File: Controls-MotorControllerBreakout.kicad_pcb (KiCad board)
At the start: 2 copper layers, 39.2 x 24.8 mm, 16 parts, among them J1 MC CAN 1, J2 MC CAN 2, J3 CAN INTRFC, J4 EXT PWR

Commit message: change diode + models
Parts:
- D2: value 1N4007 -> M7
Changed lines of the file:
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@@
 			)
 		)
-		(property "Value" "1N4007"
+		(property "Value" "M7"
 			(at 0 -2.1 0)
 			(layer "B.Fab")
@@
 			)
 		)
-		(property "Datasheet" "https://www.digikey.com/en/products/detail/smc-diode-solutions/1N4007FL/11657817"
+		(property "Datasheet" "https://www.diodes.com/assets/Datasheets/RS1MWF.pdf"
 			(at 0 0 0)
 			(unlocked yes)
@@
 			)
 		)
-		(property "P/N" "1N4007FL"
+		(property "P/N" "RS1MWF-7"
 			(at 0 0 0)
 			(unlocked yes)

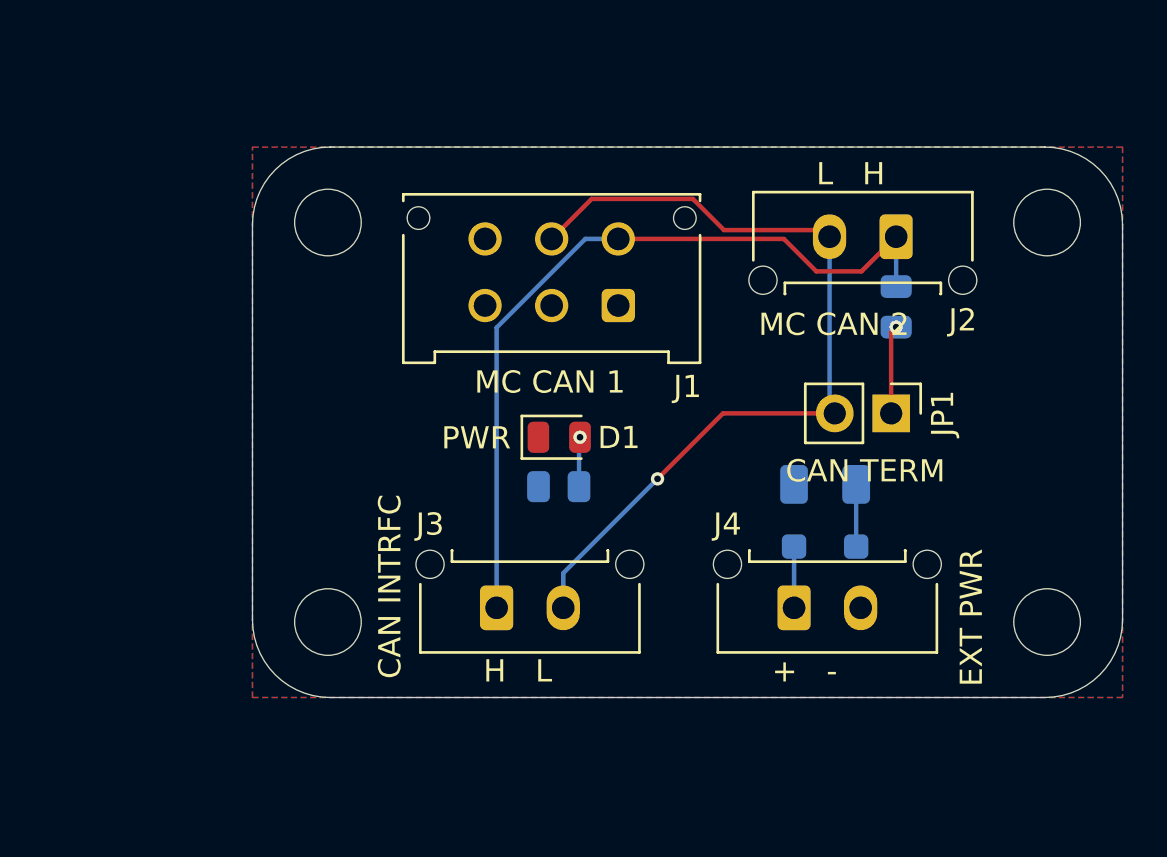
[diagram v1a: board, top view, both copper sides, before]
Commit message: fix PP & add dsub conn
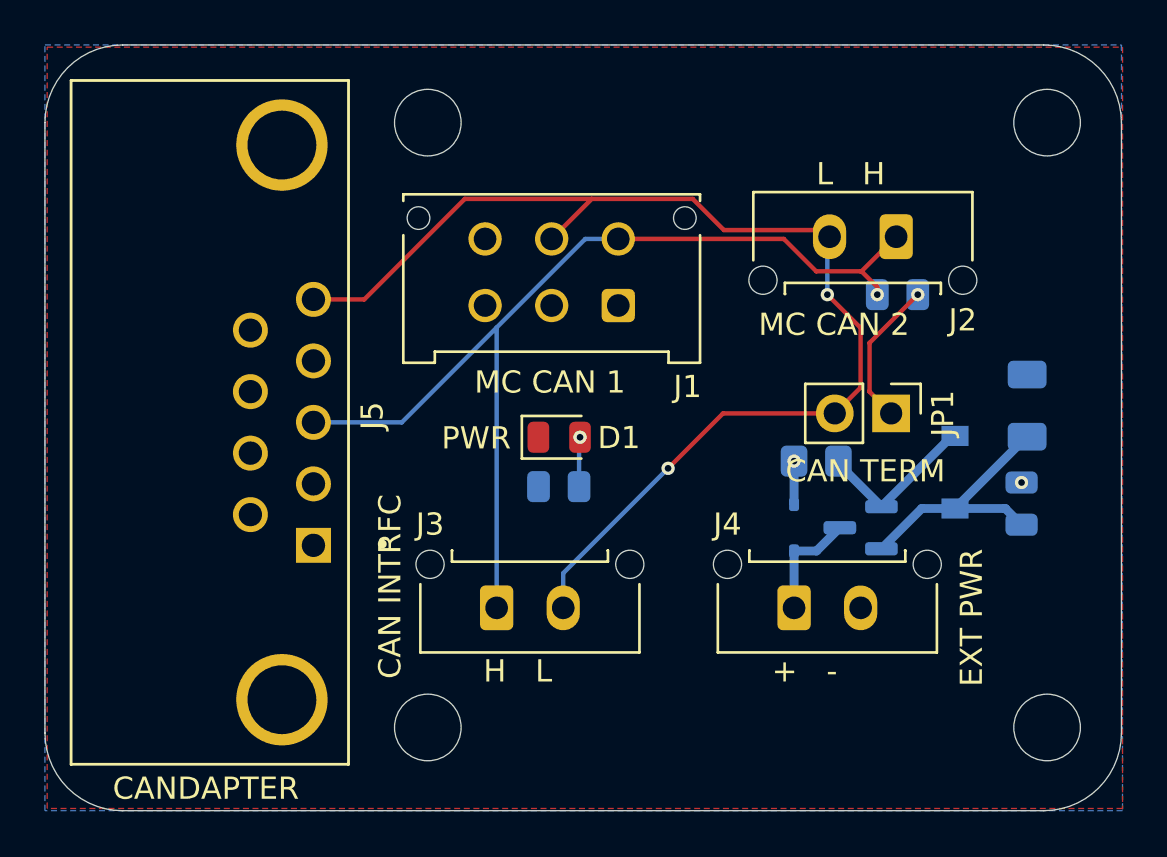
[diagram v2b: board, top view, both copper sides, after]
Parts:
- added C1: 10u, Capacitor_SMD:C_0805_2012Metric, B.Cu at (148.2, 55.7)
- added J5: CANDAPTER, DB-9 Connector:AMPHENOL_L77SDE09SA4CH3R, F.Cu at (114.9, 52.0)
- added Q1: PMV35EPER, Package_TO_SOT_SMD:SOT-23, B.Cu at (141.0, 56.8)
- added R3: 100k, Resistor_SMD:R_0805_2012Metric_Pad1.20x1.40mm_HandSolder, B.Cu at (139.0, 53.8)
- added Z1: BZT52-B12-QX, Zener:BZT52B12QX, B.Cu at (145.2, 54.2)
- D2: value M7 -> SD12_SOD323; footprint Diode_SMD:D_SOD-123F -> Diode_SMD:D_SOD-323
- F1: value Fuse -> 375mA
- moved LOGO1 12.1 mm to (108.5, 52.5)
- moved F1 9.77 mm to (148.5, 51.2), turned to 90 degrees
- moved H3 6.54 mm to (121.5, 65.8)
- moved H1 6.36 mm to (121.5, 38.5)
- moved H4 4.75 mm to (149.4, 65.8)
- moved H2 4.50 mm to (149.4, 38.5)
- moved D2 1.64 mm to (138.0, 56.8), turned to -90 degrees
- moved R1 0.55 mm to (142.7, 46.2), turned to 180 degrees
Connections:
- D2 pad 1: Net-(D2-K) -> GND
- F1 pad 1: +12V -> Net-(Q1-S)
- F1 pad 2: Net-(D2-K) -> +12V
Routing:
- net /CAN_L: track 38.8 -> 54.3 mm, vias 1 -> 2
- net Net-(Q1-S): track 0.00 -> 12.0 mm
- net /CAN_H: track 35.8 -> 44.9 mm, vias 0 -> 1
- net Net-(Q1-G): track 0.00 -> 7.48 mm
- net Net-(D2-K): track 2.80 -> 0.00 mm
- net Net-(JP1-A): track 4.30 -> 6.66 mm
- net /EXT_PWR: track 2.76 -> 5.06 mm
- net GND: track 0.00 -> 1.95 mm, vias 0 -> 2
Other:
- board size 39.2 x 24.8 mm -> 48.5 x 34.5 mm

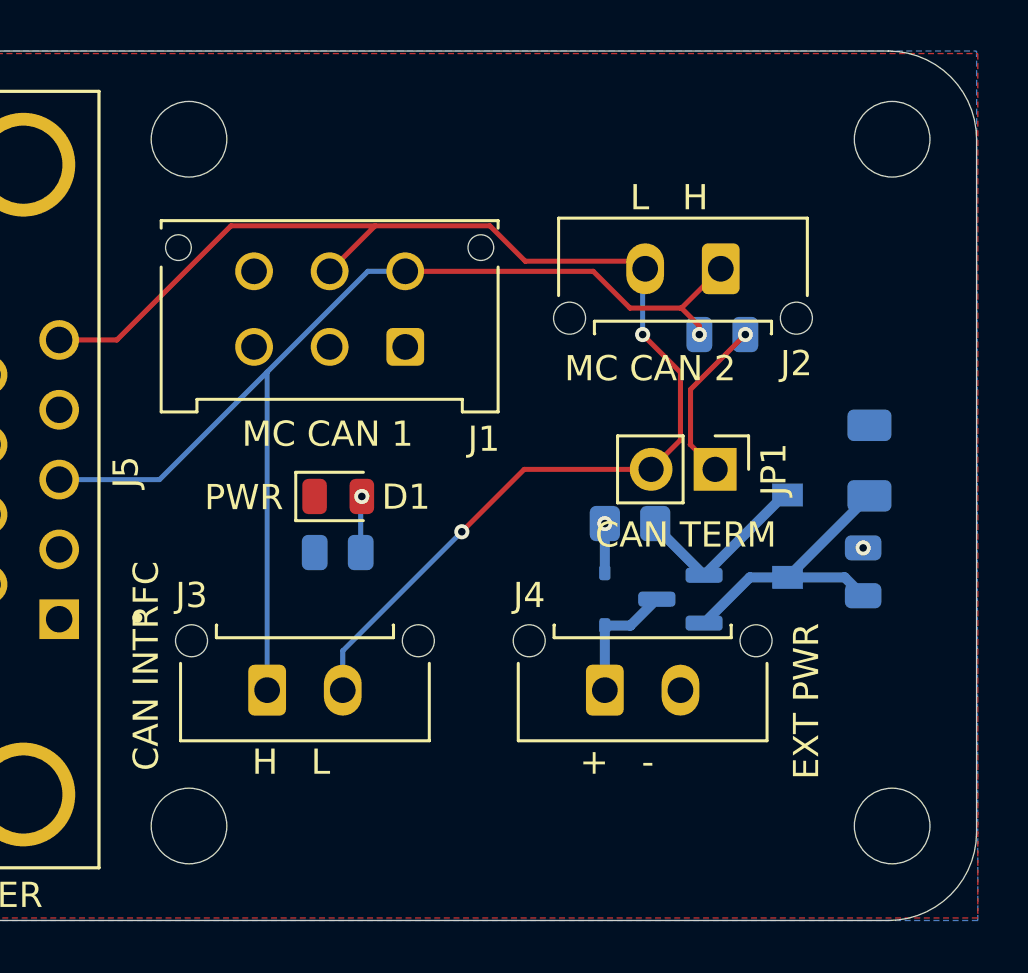
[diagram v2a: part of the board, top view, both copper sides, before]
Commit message: rm mountingholes
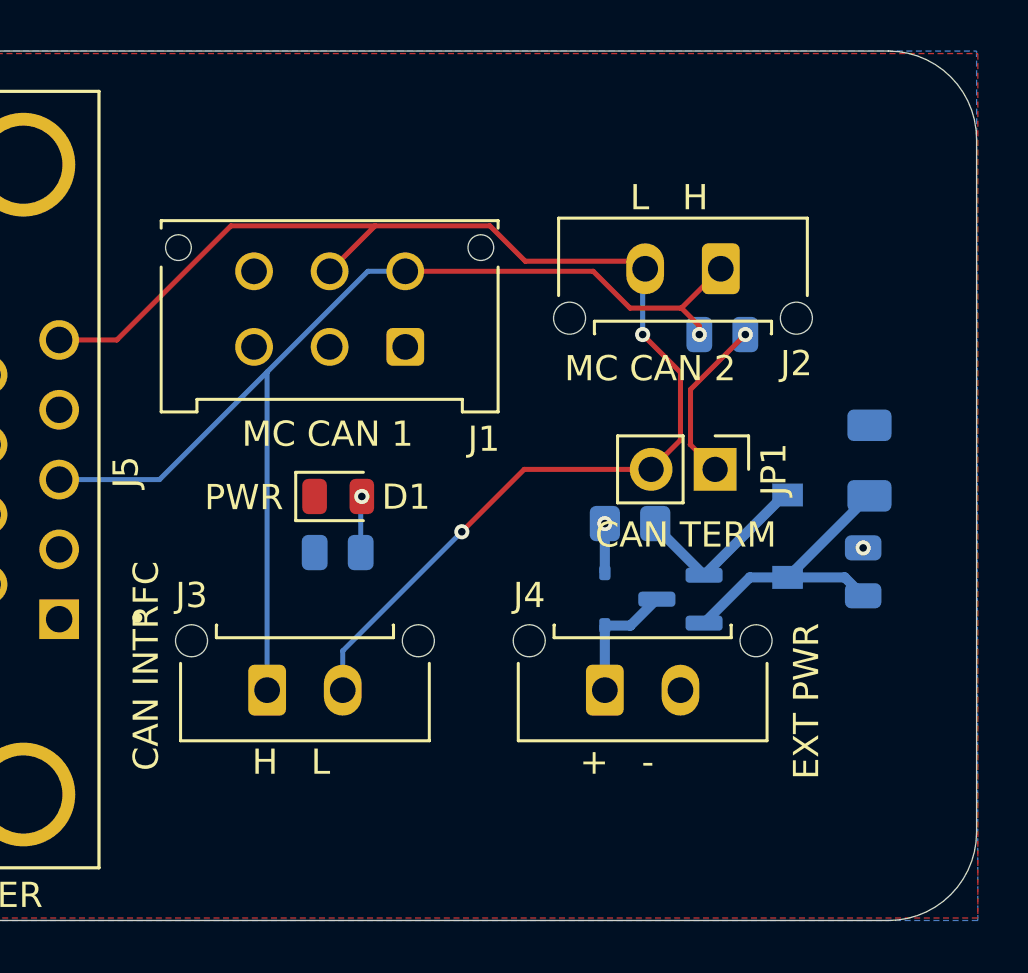
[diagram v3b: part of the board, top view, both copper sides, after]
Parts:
- removed H1, H2, H3, H4: M3, MountingHole:MountingHole_3mm

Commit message: gerbs + bom
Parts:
- moved D1 15.3 mm to (132.8, 67.0)
- moved R2 11.2 mm to (132.8, 64.8)
- moved G*** 2.71 mm to (135.0, 50.0)
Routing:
- net /CAN_H: track 44.9 -> 42.4 mm
- net /CAN_L: track 54.3 -> 53.2 mm
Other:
- board text added: "Grid size is 0.25mm"
- board text added: "profinity/controls pls work :)"

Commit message: layout kinda screwy but it works?
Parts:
- added C2: 0.1u, Capacitor_SMD:C_0805_2012Metric, F.Cu at (92.1, 60.2)
- added C3: 0.1u, Capacitor_SMD:C_0805_2012Metric, F.Cu at (96.2, 65.2)
- added C4: 0.1u, Capacitor_SMD:C_0805_2012Metric, F.Cu at (91.2, 63.2)
- added C5: 1u, Capacitor_SMD:C_0805_2012Metric, F.Cu at (96.2, 61.5)
- added D3: CTRLS, LED_SMD:LED_0805_2012Metric, F.Cu at (112.2, 63.2)
- added D4: EXT, LED_SMD:LED_0805_2012Metric, F.Cu at (112.2, 65.8)
- added H1: MountingHole, MountingHole:MountingHole_3mm, F.Cu at (75.8, 47.2)
- added H2: MountingHole, MountingHole:MountingHole_3mm, F.Cu at (75.8, 85.2)
- added H3: MountingHole, MountingHole:MountingHole_3mm, F.Cu at (117.0, 85.2)
- added H4: MountingHole, MountingHole:MountingHole_3mm, F.Cu at (117.0, 47.2)
- added JP2: EXT ENABLE, Connector_PinHeader_2.54mm:PinHeader_1x02_P2.54mm_Vertical, F.Cu at (103.8, 76.0)
- added LOGO2: Hallock, UTSVT_Special:Hallock_Image_Tiny, F.Cu at (94.8, 35.3)
- added R10: 22.1k, Resistor_SMD:R_0805_2012Metric, B.Cu at (113.7, 65.8)
- added R4: 100k, Resistor_SMD:R_0805_2012Metric, B.Cu at (95.7, 58.5)
- added R5: 62k, Resistor_SMD:R_0805_2012Metric, B.Cu at (88.9, 65.2)
- added R6: 5k, Resistor_SMD:R_0805_2012Metric, B.Cu at (86.7, 65.2)
- added R7: 5k, Resistor_SMD:R_0805_2012Metric, B.Cu at (100.7, 65.2)
- added R8: 62k, Resistor_SMD:R_0805_2012Metric, B.Cu at (98.4, 65.2)
- added R9: 22.1k, Resistor_SMD:R_0805_2012Metric, B.Cu at (113.7, 63.2)
- added U1: TPS2121RUXR, TPS2121:RUX0012A, F.Cu at (93.7, 63.4)
- G***, LOGO1: moved to F.Cu
- J3: value CAN INTRFC -> CTRLS; footprint Connector_Molex:Molex_Micro-Fit_3.0_43650-0215_1x02_P3.00mm_Vertical -> Connector_Molex:Molex_Micro-Fit_3.0_43045-0612_2x03_P3.00mm_Vertical
- R3: footprint Resistor_SMD:R_0805_2012Metric_Pad1.20x1.40mm_HandSolder -> Resistor_SMD:R_0805_2012Metric
- moved R1 57.8 mm to (93.8, 77.0)
- moved G*** 53.6 mm to (84.2, 32.8), turned to 0 degrees
- moved JP1 52.6 mm to (94.5, 73.5)
- moved C1 45.2 mm to (103.9, 64.4), turned to 180 degrees
- moved F1 42.3 mm to (108.3, 64.4), turned to 0 degrees
- moved LOGO1 41.6 mm to (70.8, 35.0), turned to 0 degrees
- moved J1 38.6 mm to (91.5, 48.7), turned to 0 degrees
- moved J4 38.4 mm to (106.8, 82.8)
- moved J3 38.3 mm to (91.5, 79.6)
- moved R3 38.1 mm to (101.2, 58.4)
- moved D2 37.8 mm to (100.5, 61.5)
- moved Z1 37.7 mm to (107.9, 59.3)
- moved Q1 37.6 mm to (103.7, 61.5)
- moved J2 36.2 mm to (106.8, 48.8), turned to 0 degrees
- moved J5 35.5 mm to (82.4, 66.3)
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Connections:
- D2 pad 2: /EXT_PWR -> /PowerDist/+12V_SEL
- J3 pad 1: /CAN_H -> /+12V_CTRLS
- J3 pad 2: /CAN_L -> GND
- J4 pad 1: /EXT_PWR -> /+12V_EXT
- Q1 pad 3: /EXT_PWR -> /PowerDist/+12V_SEL
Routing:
- net /CAN_L: track 53.2 -> 0.00 mm, vias 2 -> 0
- net /CAN_H: track 42.4 -> 0.00 mm, vias 1 -> 0
- net /PowerDist/OV2: track 0.00 -> 8.39 mm, vias 0 -> 1
- net /PowerDist/OV1: track 0.00 -> 8.39 mm, vias 0 -> 1
- net Net-(JP1-A): track 6.66 -> 0.00 mm, vias 1 -> 0
- net GND: track 1.95 -> 8.43 mm, vias 2 -> 5
- net /EXT_PWR: track 5.06 -> 0.00 mm
- net /PowerDist/ILM: track 0.00 -> 4.05 mm, vias 0 -> 1
- net Net-(Q1-S): track 12.0 -> 8.01 mm
- net /PowerDist/+12V_SEL: track 0.00 -> 2.75 mm, vias 0 -> 3
- net /PowerDist/CSS: track 0.00 -> 2.09 mm
- net Net-(D4-A): track 0.00 -> 1.53 mm, vias 0 -> 1
- net Net-(D3-A): track 0.00 -> 1.53 mm, vias 0 -> 1
- net Net-(D1-A): track 2.32 -> 1.53 mm
- net /PowerDist/+12V_EXT_EN: vias 0 -> 3
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- added copper zone on B.Cu, net /+12V_CTRLS
- added copper zone on F.Cu, net /+12V_CTRLS
- added copper zone on B.Cu, net /PowerDist/+12V_EXT_EN
- added copper zone on F.Cu, net /PowerDist/+12V_EXT_EN
- added copper zone on B.Cu, net /PowerDist/+12V_SEL
- added copper zone on F.Cu, net /PowerDist/+12V_SEL
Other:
- board size 48.5 x 34.5 mm -> 47.8 x 44.5 mm
- board text added: "PWR STATUS"
- board text added: "TODO: add back all useful labels and stuff from v1"
- board text removed: "L H"
- board text removed: "Motor Controller Breakout"
- board text removed: "PWR"
- board text removed: "Ravi Shah 2024"
- board text removed: "profinity/controls pls work :)"

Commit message: initial layout
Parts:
- removed LOGO2: Hallock, UTSVT_Special:Hallock_Image_Tiny
- added G***: LOGO, LOGO, B.Cu at (113.8, 73.0)
- LOGO1: moved to B.Cu
- moved LOGO1 31.5 mm to (76.5, 66.0), turned to 90 degrees
- moved G*** 15.1 mm to (82.5, 47.8)
- moved F1 8.28 mm to (111.5, 56.8), turned to 90 degrees
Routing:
- net /CAN_L: track 0.00 -> 73.9 mm, vias 0 -> 2
- net /CAN_H: track 0.00 -> 62.8 mm, vias 0 -> 2
- net /+12V_STATUS: track 0.00 -> 32.7 mm, vias 0 -> 2
- net Net-(Q1-S): track 8.01 -> 2.91 mm
- net Net-(JP1-A): track 0.00 -> 3.55 mm
- net /PowerDist/+12V_SEL: track 2.75 -> 0.00 mm, vias 3 -> 8
- net /PowerDist/+12V_EXT_EN: vias 3 -> 7
- net /+12V_CTRLS: vias 3 -> 7
- added copper zone on B.Cu, net /+12V_EXT
- added copper zone on B.Cu, net Net-(Q1-S)
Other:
- board text added: "Motor Controller Breakout"
- board text added: "Ravi Shah 2024"
- board text added: "TODO: add space on board to VHB motor interface board (custom footprint 5.5 x 2.5cm)"
- board text added: "daybreak pls work :)"
- board text added: "v2.0"
- board text removed: "TODO: add back all useful labels and stuff from v1"

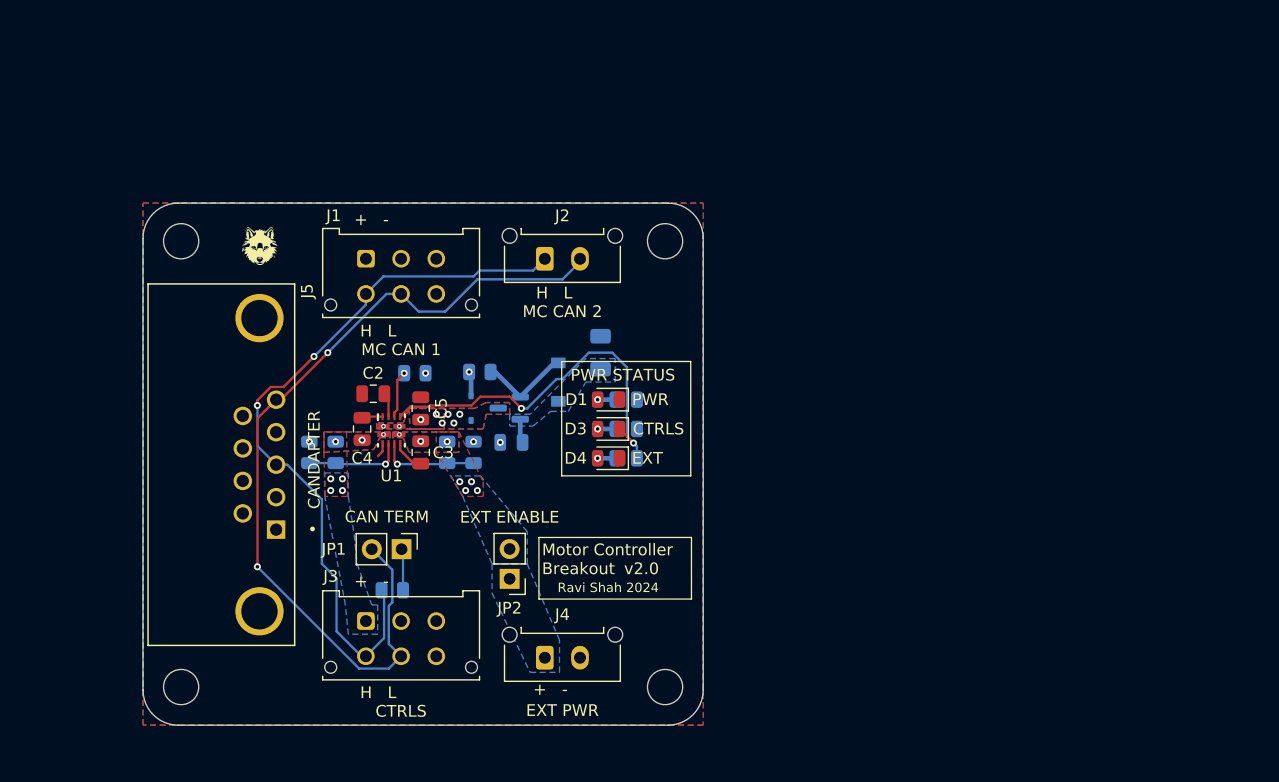
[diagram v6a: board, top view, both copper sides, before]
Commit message: mc interface footprint & better input pours
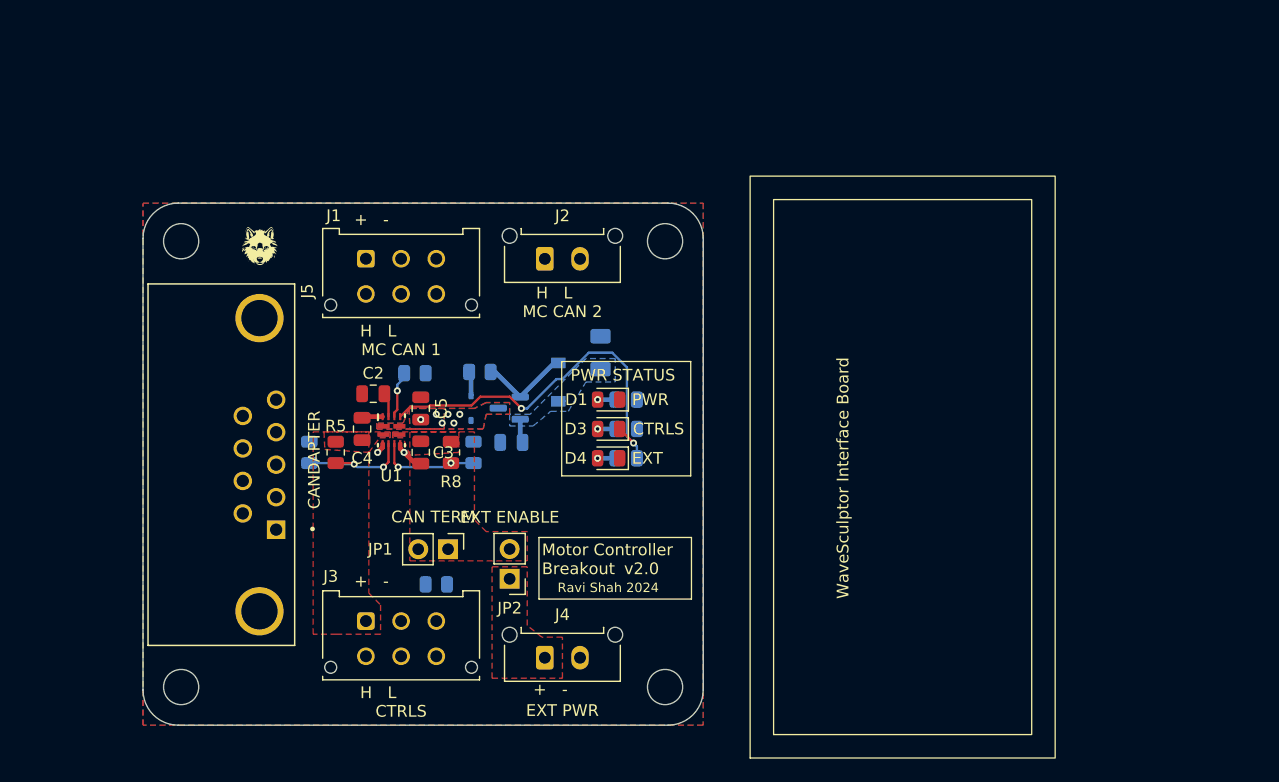
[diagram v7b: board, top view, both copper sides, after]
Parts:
- added LOGO2: WS Motor Interface, Wavesculptor_Motor_Interface:Wavesculptor_Motor_Interface_Type_1, F.Cu at (137.2, 66.5)
- R5, R8: moved to F.Cu
- moved JP1 3.96 mm to (98.5, 73.5)
- moved R1 3.78 mm to (97.5, 76.5)
- moved R8 0.33 mm to (98.8, 65.2)
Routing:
- net /CAN_L: track 73.9 -> 0.66 mm, vias 2 -> 0
- net /CAN_H: track 62.8 -> 0.37 mm, vias 2 -> 0
- net Net-(JP1-A): track 3.55 -> 0.34 mm
- net /PowerDist/OV2: track 8.39 -> 10.3 mm, vias 1 -> 2
- net /PowerDist/OV1: track 8.39 -> 8.70 mm, vias 1 -> 2
- net GND: track 8.43 -> 8.67 mm, vias 5 -> 2
- net /PowerDist/+12V_SEL: vias 8 -> 6
- net /PowerDist/+12V_EXT_EN: vias 7 -> 0
- net /+12V_CTRLS: vias 7 -> 0
- added copper zone on F.Cu, net /+12V_EXT
- added copper zone on B.Cu, net GND
- removed copper zone on B.Cu, net +12V
- removed copper zone on B.Cu, net /+12V_CTRLS
- removed copper zone on B.Cu, net /+12V_EXT
- removed copper zone on B.Cu, net /PowerDist/+12V_EXT_EN
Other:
- board text removed: "TODO: add space on board to VHB motor interface board (custom footprint 5.5 x 2.5cm)"
